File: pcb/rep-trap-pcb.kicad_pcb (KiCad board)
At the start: 4 copper layers, 161 x 23 mm, 82 parts, among them J1 BATT+, J2 GND, J3 USB4105-GF-A, J4 VBUS, J5 SJ2-25773B-SMT-TR, J6 S2B-PH-K/DNP, J7 GND, SW1 SKRKAEE020, SW2 SKRKAEE020, U1 AP2112K-3.3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

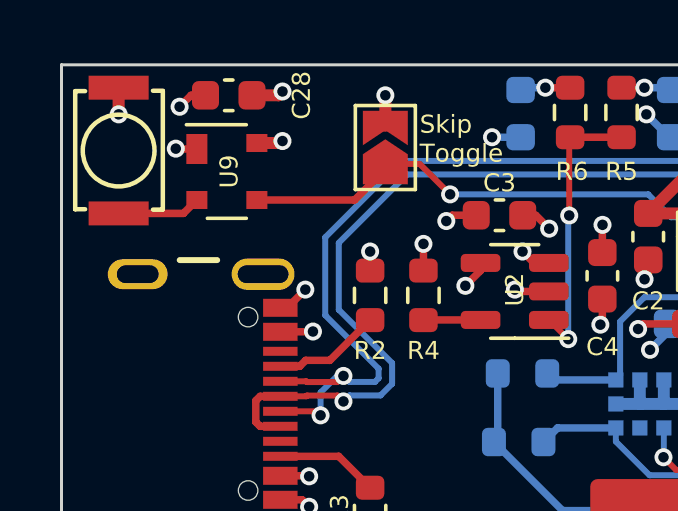
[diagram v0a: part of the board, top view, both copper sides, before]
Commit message: Removed debounce IC and replaced with default on off switch
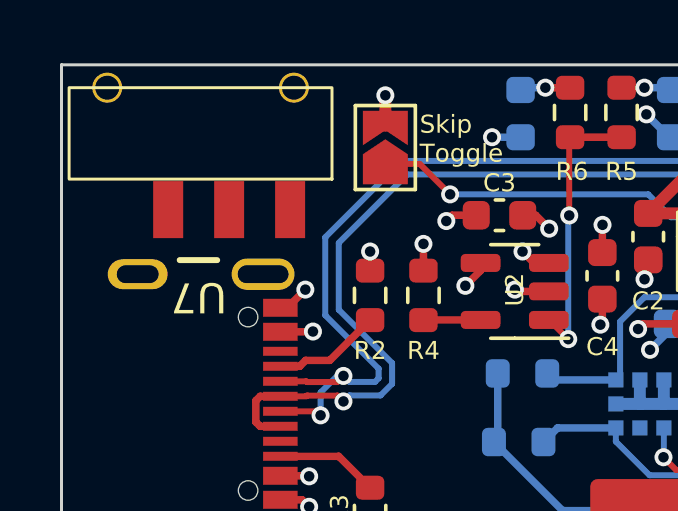
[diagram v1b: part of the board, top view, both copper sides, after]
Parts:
- removed C28: 0.1µF, Capacitor_SMD:C_0603_1608Metric
- removed SW2: SKRKAEE020, SKRKAEE020:SKRKAEE020
- removed U9: MAX6816, Package_TO_SOT_SMD:SOT-143
- added U7: 450405020524, 450405020524:450405020524, F.Cu at (73.8, 80.0)
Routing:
- net /main/ENABLE: track 19.2 -> 14.5 mm
- net +BATT: track 37.2 -> 34.4 mm, vias 17 -> 14
- net Net-(U9-IN): track 2.79 -> 0.00 mm
- net GND: track 103.5 -> 101.7 mm, vias 66 -> 64

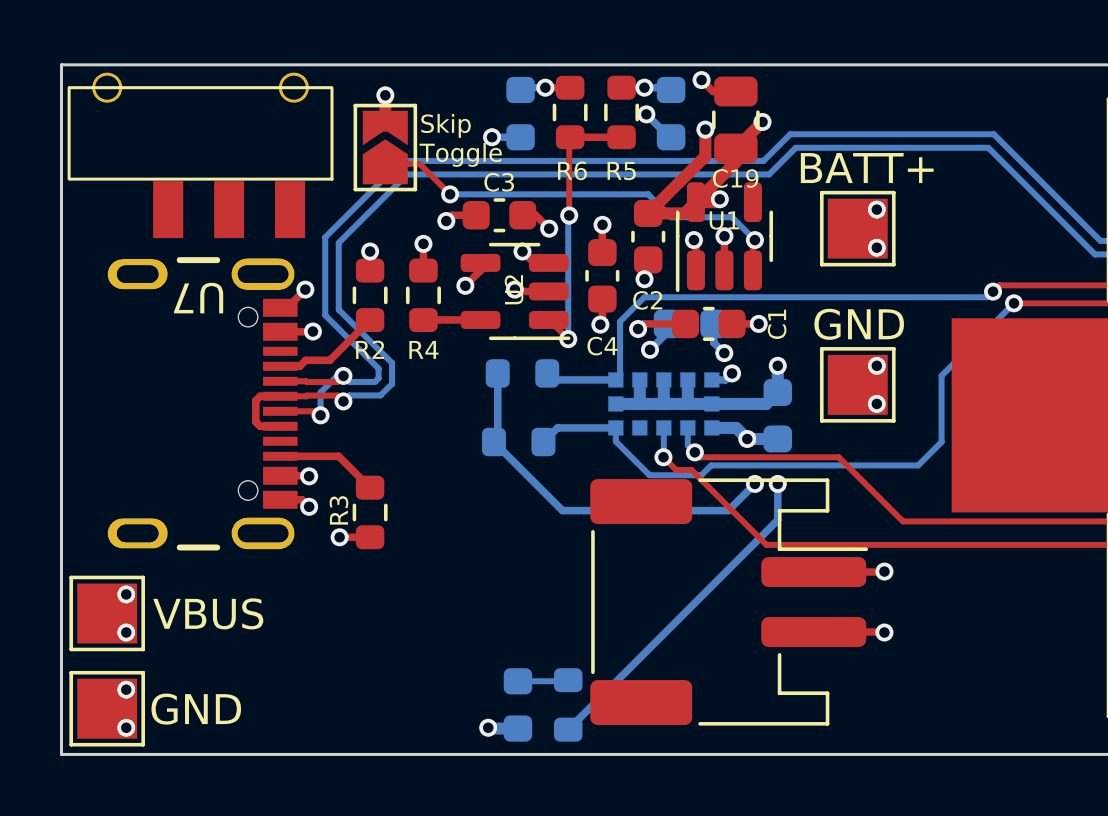
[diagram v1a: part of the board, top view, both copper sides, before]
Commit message: Applied ERC issue changes + DRC issues fix
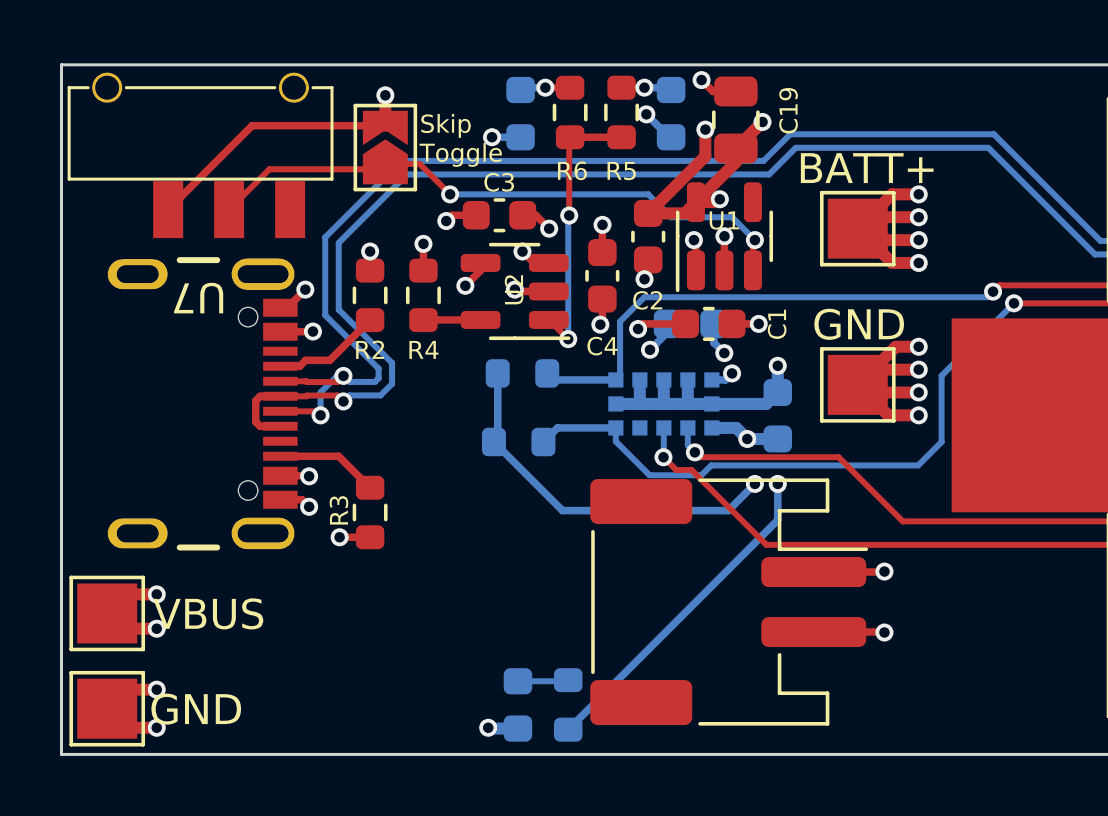
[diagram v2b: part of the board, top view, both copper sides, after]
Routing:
- net +BATT: track 34.4 -> 52.2 mm, vias 14 -> 16
- net GND: track 101.7 -> 115.0 mm, vias 64 -> 66
- net /main/ENABLE: track 14.5 -> 20.2 mm
- net VBUS: track 4.11 -> 7.88 mm

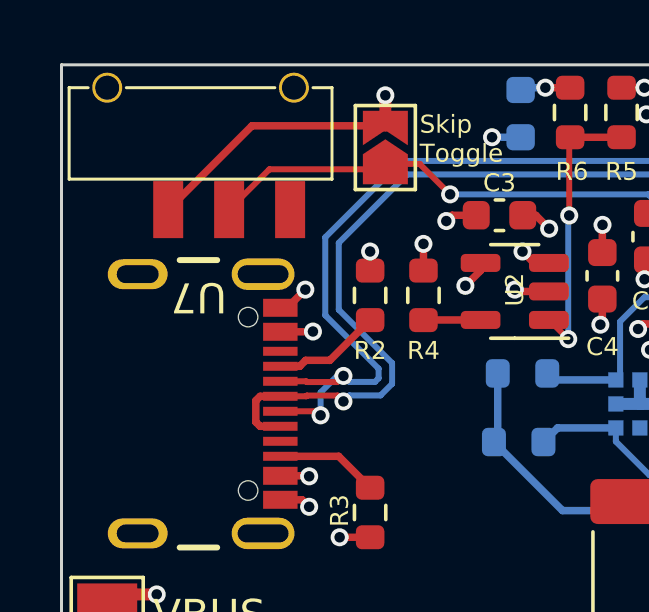
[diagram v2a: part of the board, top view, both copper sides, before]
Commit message: Added basic kibot config
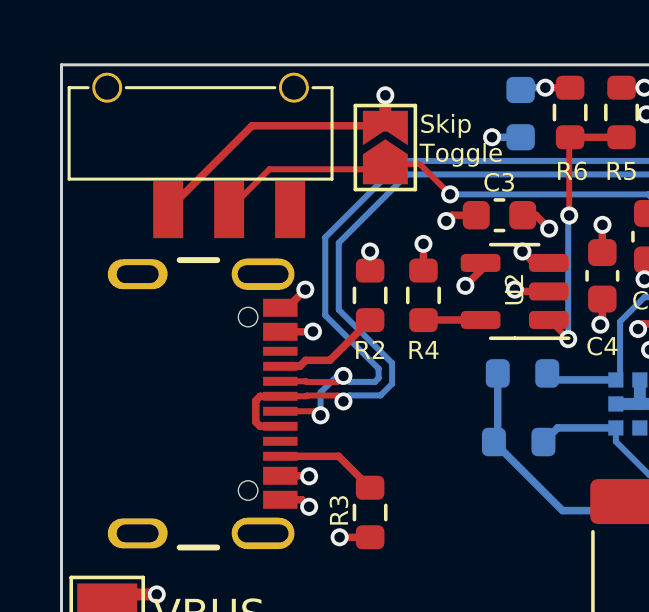
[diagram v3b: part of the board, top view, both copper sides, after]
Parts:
- renumbered G*** to G1
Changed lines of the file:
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@@
     (clearance 0.1)
     (attr smd)
-    (fp_text reference "J3" (at -1.825 -8.135 90) (layer "F.SilkS") hide
+    (fp_text reference "J3" (at 0.893 -1.905 90) (layer "F.SilkS") hide
         (effects (font (size 1 1) (thickness 0.015)))
     )
-    (fp_text value "USB4105-GF-A" (at 0.131 3.683 90) (layer "F.Fab")
+    (fp_text value "USB4105-GF-A" (at 0.893 -1.905 90) (layer "F.Fab") hide
         (effects (font (size 1 1) (thickness 0.015)))
     )
@@
     (property "Sheetname" "main")
     (attr smd)
-    (fp_text reference "U7" (at 0 -6.985 180 unlocked) (layer "F.SilkS")
+    (fp_text reference "U7" (at 0.127 -1.27 180 unlocked) (layer "F.SilkS") hide
         (effects (font (size 1 1) (thickness 0.1)))
     )
@@
   (footprint "LOGO" (layer "B.Cu")
     (at 149.95865 97.687859 180)
-    (attr board_only exclude_from_pos_files exclude_from_bom)
-    (fp_text reference "G***" (at 0 0) (layer "B.SilkS") hide
+    (attr board_only)
+    (fp_text reference "G1" (at 0 0) (layer "B.SilkS") hide
         (effects (font (size 1.5 1.5) (thickness 0.3)) (justify mirror))
     )
@@
     (pts (xy 230.124 79.248) (xy 69.215 79.248))
     (height 11.7856)
-    (gr_text "160.9090 mm" (at 149.6695 65.6624) (layer "F.Cu")
+    (gr_text "160,9090 mm" (at 149.6695 65.6624) (layer "F.Cu")
       (effects (font (size 1.5 1.5) (thickness 0.3)))
     )
@@
     (pts (xy 230.124 102.235) (xy 230.124 79.248))
     (height 14.0208)
-    (gr_text "22.9870 mm" (at 242.3448 90.7415 90) (layer "F.Cu")
+    (gr_text "22,9870 mm" (at 242.3448 90.7415 90) (layer "F.Cu")
       (effects (font (size 1.5 1.5) (thickness 0.3)))
     )

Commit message: Added notes and ToDos to be worked on for REV.02
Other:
- board text added: "- all connectors on one side (USB, Klinke) - exchange 18650 Battery Holder crap - apply heatsink guidelines to charger IC - number sensors"
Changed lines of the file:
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@@
     (effects (font (size 0.6 0.6) (thickness 0.15)) (justify left bottom))
+  )
+  (gr_text "- all connectors on one side (USB, Klinke)\n- exchange 18650 Battery Holder crap\n- apply heatsink guidelines to charger IC\n- number sensors " (at 111.887 125.603) (layer "Dwgs.User")
+    (effects (font (size 3 3) (thickness 0.3) bold) (justify left bottom))
   )
   (dimension (type aligned) (layer "F.Cu")
     (pts (xy 230.124 79.248) (xy 69.215 79.248))
     (height 11.7856)
-    (gr_text "160,9090 mm" (at 149.6695 65.6624) (layer "F.Cu")
+    (gr_text "160.9090 mm" (at 149.6695 65.6624) (layer "F.Cu")
       (effects (font (size 1.5 1.5) (thickness 0.3)))
     )
@@
     (pts (xy 230.124 102.235) (xy 230.124 79.248))
     (height 14.0208)
-    (gr_text "22,9870 mm" (at 242.3448 90.7415 90) (layer "F.Cu")
+    (gr_text "22.9870 mm" (at 242.3448 90.7415 90) (layer "F.Cu")
       (effects (font (size 1.5 1.5) (thickness 0.3)))
     )
@@
   (via (at 82.677 86.614) (size 0.6) (drill 0.35) (layers "F.Cu" "B.Cu") (net 4))
   (segment (start 191.855 100.641) (end 193.253 100.641) (width 0.2) (layer "F.Cu") (net 5))
+  (segment (start 199.617746 95.124503) (end 199.60439 95.124503) (width 0.2) (layer "F.Cu") (net 5))
+  (segment (start 199.377 96.152) (end 198.755 96.774) (width 0.2) (layer "F.Cu") (net 5))
+  (segment (start 191.135 99.921) (end 191.855 100.641) (width 0.2) (layer "F.Cu") (net 5))
+  (segment (start 198.755 96.774) (end 196.92 96.774) (width 0.2) (layer "F.Cu") (net 5))
+  (segment (start 199.377 95.351893) (end 199.377 96.152) (width 0.2) (layer "F.Cu") (net 5))
+  (segment (start 193.253 100.441) (end 193.253 100.641) (width 0.2) (layer "F.Cu") (net 5))
+  (segment (start 200.057 94.685249) (end 199.617746 95.124503) (width 0.2) (layer "F.Cu") (net 5))
+  (segment (start 196.92 96.774) (end 193.253 100.441) (width 0.2) (layer "F.Cu") (net 5))
+  (segment (start 200.057 93.9885) (end 200.057 94.685249) (width 0.2) (layer "F.Cu") (net 5))
   (segment (start 199.60439 95.124503) (end 199.377 95.351893) (width 0.2) (layer "F.Cu") (net 5))
-  (segment (start 196.92 96.774) (end 193.253 100.441) (width 0.2) (layer "F.Cu") (net 5))
-  (segment (start 191.135 99.921) (end 191.855 100.641) (width 0.2) (layer "F.Cu") (net 5))
-  (segment (start 200.057 94.685249) (end 199.617746 95.124503) (width 0.2) (layer "F.Cu") (net 5))
-  (segment (start 193.253 100.441) (end 193.253 100.641) (width 0.2) (layer "F.Cu") (net 5))
-  (segment (start 199.377 96.152) (end 198.755 96.774) (width 0.2) (layer "F.Cu") (net 5))
-  (segment (start 200.057 93.9885) (end 200.057 94.685249) (width 0.2) (layer "F.Cu") (net 5))
-  (segment (start 198.755 96.774) (end 196.92 96.774) (width 0.2) (layer "F.Cu") (net 5))
-  (segment (start 199.617746 95.124503) (end 199.60439 95.124503) (width 0.2) (layer "F.Cu") (net 5))
-  (segment (start 199.377 95.351893) (end 199.377 96.152) (width 0.2) (layer "F.Cu") (net 5))
   (segment (start 200.152 98.326) (end 199.898 98.58) (width 0.2) (layer "F.Cu") (net 6))
   (segment (start 200.152 97.409) (end 200.152 98.326) (width 0.2) (layer "F.Cu") (net 6))
@@
   (segment (start 204.0945 88.751) (end 210.08 88.751) (width 0.2) (layer "F.Cu") (net 50))
   (segment (start 210.08 88.751) (end 212.345 86.486) (width 0.2) (layer "F.Cu") (net 50))
-  (segment (start 203.044254 96.3135) (end 207.441754 100.711) (width 0.2) (layer "F.Cu") (net 51))
+  (segment (start 201.657 93.9885) (end 201.657 94.926246) (width 0.2) (layer "F.Cu") (net 51))
   (segment (start 207.441754 100.711) (end 207.518 100.711) (width 0.2) (layer "F.Cu") (net 51))
-  (segment (start 201.657 94.96396) (end 201.892998 95.199958) (width 0.2) (layer "F.Cu") (net 51))
-  (segment (start 201.892998 95.326958) (end 202.87954 96.3135) (width 0.2) (layer "F.Cu") (net 51))
-  (segment (start 202.87954 96.3135) (end 203.044254 96.3135) (width 0.2) (layer "F.Cu") (net 51))
-  (segment (start 201.657 93.9885) (end 201.657 94.96396) (width 0.2) (layer "F.Cu") (net 51))
-  (segment (start 201.892998 95.199958) (end 201.892998 95.326958) (width 0.2) (layer "F.Cu") (net 51))
-  (segment (start 207.083075 99.661) (end 209.643 99.661) (width 0.2) (layer "F.Cu") (net 52))
-  (segment (start 207.05756 99.686515) (end 207.083075 99.661) (width 0.2) (layer "F.Cu") (net 52))
-  (segment (start 210.312 100.33) (end 210.312 100.711) (width 0.2) (layer "F.Cu") (net 52))
-  (segment (start 206.982249 99.686515) (end 207.05756 99.686515) (width 0.2) (layer "F.Cu") (net 52))
-  (segment (start 202.057 94.761266) (end 206.982249 99.686515) (width 0.2) (layer "F.Cu") (net 52))
-  (segment (start 209.643 99.661) (end 210.312 100.33) (width 0.2) (layer "F.Cu") (net 52))
-  (segment (start 202.057 93.9885) (end 202.057 94.761266) (width 0.2) (layer "F.Cu") (net 52))
+  (segment (start 201.657 94.926246) (end 207.441754 100.711) (width 0.2) (layer "F.Cu") (net 51))
+  (segment (start 209.061 99.46) (end 210.312 100.711) (width 0.2) (layer "F.Cu") (net 52))
+  (segment (start 202.057 94.686661) (end 206.83034 99.46) (width 0.2) (layer "F.Cu") (net 52))
+  (segment (start 206.83034 99.46) (end 209.061 99.46) (width 0.2) (layer "F.Cu") (net 52))
+  (segment (start 202.057 93.9885) (end 202.057 94.686661) (width 0.2) (layer "F.Cu") (net 52))
   (segment (start 198.251975 86.376) (end 198.456839 86.580864) (width 0.2) (layer "F.Cu") (net 56))
   (segment (start 189.611 83.312) (end 191.77 85.471) (width 0.2) (layer "F.Cu") (net 56))
@@
   (segment (start 195.58 83.312) (end 197.044998 84.776998) (width 0.2) (layer "F.Cu") (net 60))
   (segment (start 197.044998 84.776998) (end 198.91501 84.776998) (width 0.2) (layer "F.Cu") (net 60))
-  (segment (start 202.457 94.520975) (end 207.197524 99.261499) (width 0.2) (layer "F.Cu") (net 66))
-  (segment (start 207.197524 99.261499) (end 211.656499 99.261499) (width 0.2) (layer "F.Cu") (net 66))
-  (segment (start 211.656499 99.261499) (end 213.106 100.711) (width 0.2) (layer "F.Cu") (net 66))
+  (segment (start 211.455 99.06) (end 213.106 100.711) (width 0.2) (layer "F.Cu") (net 66))
+  (segment (start 202.457 94.520975) (end 206.996025 99.06) (width 0.2) (layer "F.Cu") (net 66))
+  (segment (start 206.996025 99.06) (end 211.455 99.06) (width 0.2) (layer "F.Cu") (net 66))
   (segment (start 202.457 93.9885) (end 202.457 94.520975) (width 0.2) (layer "F.Cu") (net 66))
   (zone (net 1) (net_name "+3.3V") (layer "F.Cu") (hatch edge 0.5)
